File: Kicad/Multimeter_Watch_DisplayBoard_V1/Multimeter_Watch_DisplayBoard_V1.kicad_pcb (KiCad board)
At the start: 2 copper layers, 55 x 46 mm, 21 parts, among them J1 Conn_01x03_Male, J2 Conn_01x03_Male, J3 Conn_01x03_Male, J4 Conn_01x03_Male, Q1 A03400A N-MOS, SW1 SW_Push, SW2 SW_Push, SW3 SW_Push, SW4 SW_Push, SW5 SW_Push, SW6 SW_Push

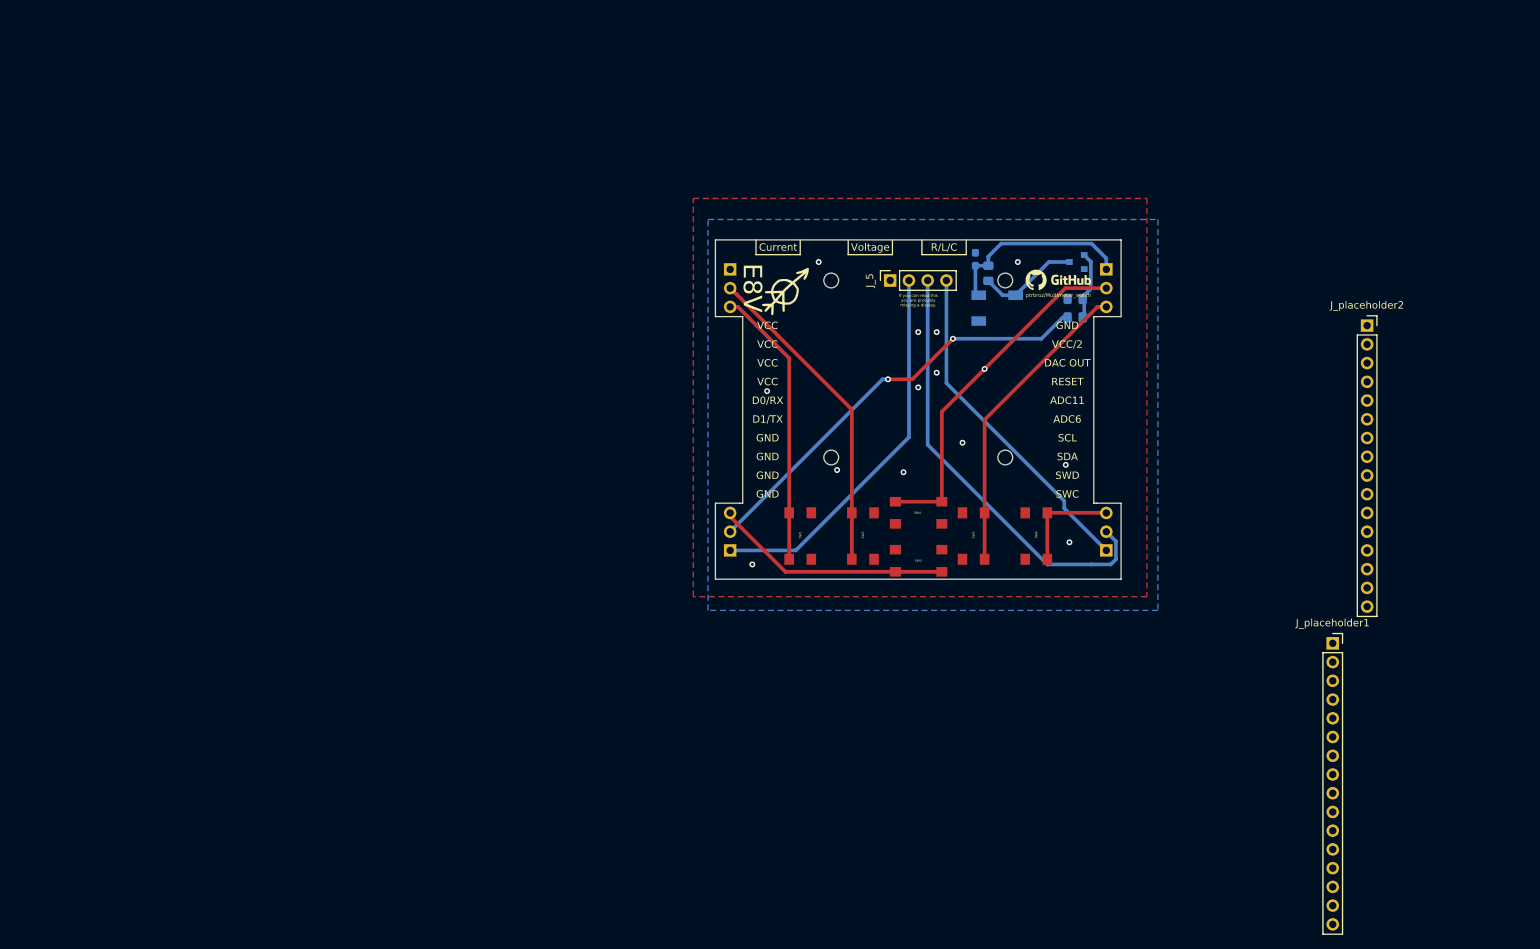
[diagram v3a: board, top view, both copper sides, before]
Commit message: Add pads on bottom of displayboard
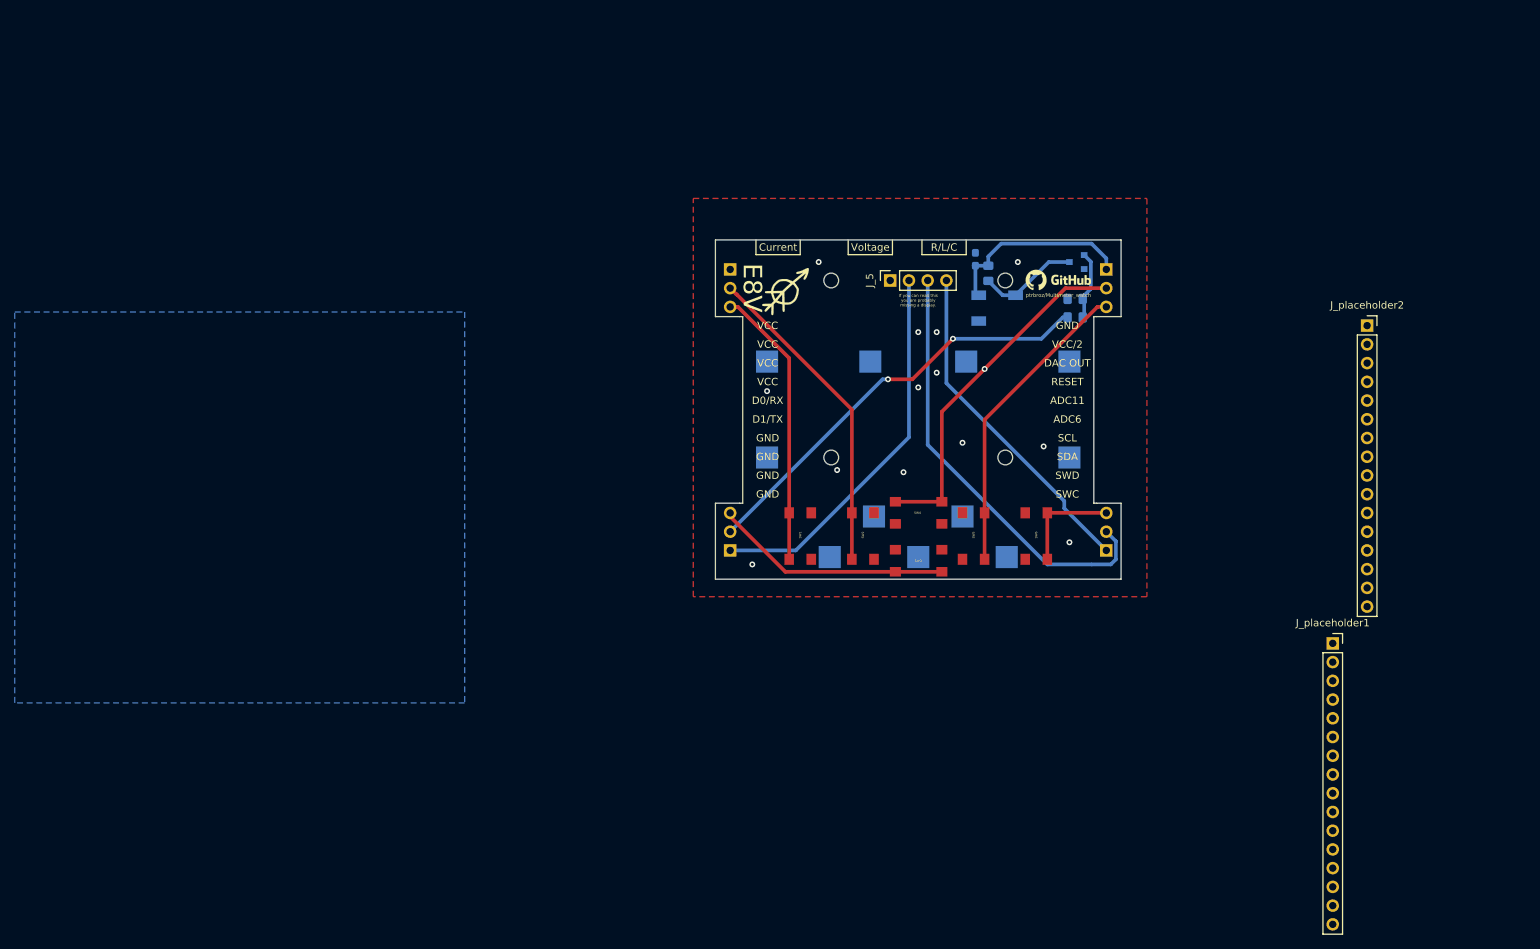
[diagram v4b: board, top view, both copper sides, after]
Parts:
- added REF**: StructPad, Multimeter_Watch_custom_footprints:StructPad, B.Cu at (137.5, 92.5)
- added REF**: StructPad, Multimeter_Watch_custom_footprints:StructPad, B.Cu at (111.0, 71.5)
- added REF**: StructPad, Multimeter_Watch_custom_footprints:StructPad, B.Cu at (152.0, 71.5)
- added REF**: StructPad, Multimeter_Watch_custom_footprints:StructPad, B.Cu at (125.5, 92.5)
- added REF**: StructPad, Multimeter_Watch_custom_footprints:StructPad, B.Cu at (125.0, 71.5)
- added REF**: StructPad, Multimeter_Watch_custom_footprints:StructPad, B.Cu at (138.0, 71.5)
- added REF**: StructPad, Multimeter_Watch_custom_footprints:StructPad, B.Cu at (131.5, 98.0)
- added REF**: StructPad, Multimeter_Watch_custom_footprints:StructPad, B.Cu at (119.5, 98.0)
- added REF**: StructPad, Multimeter_Watch_custom_footprints:StructPad, B.Cu at (143.5, 98.0)
- added REF**: StructPad, Multimeter_Watch_custom_footprints:StructPad, B.Cu at (152.0, 84.5)
- added REF**: StructPad, Multimeter_Watch_custom_footprints:StructPad, B.Cu at (111.0, 84.5)
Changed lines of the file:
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@@
   (general
     (thickness 1.6)
-    (drawings 105)
+    (drawings 106)
     (tracks 80)
     (zones 0)
-    (modules 21)
+    (modules 32)
     (nets 47)
   )
   (page A4)
   (layers
-    (0 F.Cu signal)
-    (31 B.Cu signal hide)
+    (0 F.Cu signal hide)
+    (31 B.Cu signal)
     (32 B.Adhes user hide)
     (33 F.Adhes user hide)
@@
     (38 B.Mask user hide)
     (39 F.Mask user hide)
-    (40 Dwgs.User user hide)
+    (40 Dwgs.User user)
     (41 Cmts.User user hide)
     (42 Eco1.User user)
@@
     (add_net "Net-(J_placeholder2-Pad9)")
     (add_net "Net-(Q1-Pad1)")
+  )
+  (module Multimeter_Watch_custom_footprints:StructPad (layer B.Cu)
+    (at 137.5 92.5)
+    (fp_text reference REF** (at 0 -0.5) (layer B.SilkS)
+      (effects (font (size 1 1) (thickness 0.15)) (justify mirror))
+    )
+    (fp_text value StructPad (at 0 0.5) (layer B.Fab)
+      (effects (font (size 1 1) (thickness 0.15)) (justify mirror))
+    )
+    (pad "" smd rect (at 0 0) (size 3 3) (layers B.Cu B.Paste B.Mask))
+  )
+  (module Multimeter_Watch_custom_footprints:StructPad (layer B.Cu)
+    (at 125.5 92.5)
+    (fp_text reference REF** (at 0 -0.5) (layer B.SilkS)
+      (effects (font (size 1 1) (thickness 0.15)) (justify mirror))
+    )
+    (fp_text value StructPad (at 0 0.5) (layer B.Fab)
+      (effects (font (size 1 1) (thickness 0.15)) (justify mirror))
+    )
+    (pad "" smd rect (at 0 0) (size 3 3) (layers B.Cu B.Paste B.Mask))
+  )
+  (module Multimeter_Watch_custom_footprints:StructPad (layer B.Cu)
+    (at 125 71.5)
+    (fp_text reference REF** (at 0 -0.5) (layer B.SilkS)
+      (effects (font (size 1 1) (thickness 0.15)) (justify mirror))
+    )
+    (fp_text value StructPad (at 0 0.5) (layer B.Fab)
+      (effects (font (size 1 1) (thickness 0.15)) (justify mirror))
+    )
+    (pad "" smd rect (at 0 0) (size 3 3) (layers B.Cu B.Paste B.Mask))
+  )
+  (module Multimeter_Watch_custom_footprints:StructPad (layer B.Cu)
+    (at 138 71.5)
+    (fp_text reference REF** (at 0 -0.5) (layer B.SilkS)
+      (effects (font (size 1 1) (thickness 0.15)) (justify mirror))
+    )
+    (fp_text value StructPad (at 0 0.5) (layer B.Fab)
+      (effects (font (size 1 1) (thickness 0.15)) (justify mirror))
+    )
+    (pad "" smd rect (at 0 0) (size 3 3) (layers B.Cu B.Paste B.Mask))
+  )
+  (module Multimeter_Watch_custom_footprints:StructPad (layer B.Cu)
+    (at 131.5 98)
+    (fp_text reference REF** (at 0 -0.5) (layer B.SilkS)
+      (effects (font (size 1 1) (thickness 0.15)) (justify mirror))
+    )
+    (fp_text value StructPad (at 0 0.5) (layer B.Fab)
+      (effects (font (size 1 1) (thickness 0.15)) (justify mirror))
+    )
+    (pad "" smd rect (at 0 0) (size 3 3) (layers B.Cu B.Paste B.Mask))
+  )
+  (module Multimeter_Watch_custom_footprints:StructPad (layer B.Cu)
+    (at 119.5 98)
+    (fp_text reference REF** (at 0 -0.5) (layer B.SilkS)
+      (effects (font (size 1 1) (thickness 0.15)) (justify mirror))
+    )
+    (fp_text value StructPad (at 0 0.5) (layer B.Fab)
+      (effects (font (size 1 1) (thickness 0.15)) (justify mirror))
+    )
+    (pad "" smd rect (at 0 0) (size 3 3) (layers B.Cu B.Paste B.Mask))
+  )
+  (module Multimeter_Watch_custom_footprints:StructPad (layer B.Cu)
+    (at 143.5 98)
+    (fp_text reference REF** (at 0 -0.5) (layer B.SilkS)
+      (effects (font (size 1 1) (thickness 0.15)) (justify mirror))
+    )
+    (fp_text value StructPad (at 0 0.5) (layer B.Fab)
+      (effects (font (size 1 1) (thickness 0.15)) (justify mirror))
+    )
+    (pad "" smd rect (at 0 0) (size 3 3) (layers B.Cu B.Paste B.Mask))
+  )
+  (module Multimeter_Watch_custom_footprints:StructPad (layer B.Cu)
+    (at 152 84.5)
+    (fp_text reference REF** (at 0 -0.5) (layer B.SilkS)
+      (effects (font (size 1 1) (thickness 0.15)) (justify mirror))
+    )
+    (fp_text value StructPad (at 0 0.5) (layer B.Fab)
+      (effects (font (size 1 1) (thickness 0.15)) (justify mirror))
+    )
+    (pad "" smd rect (at 0 0) (size 3 3) (layers B.Cu B.Paste B.Mask))
+  )
+  (module Multimeter_Watch_custom_footprints:StructPad (layer B.Cu)
+    (at 111 84.5)
+    (fp_text reference REF** (at 0 -0.5) (layer B.SilkS)
+      (effects (font (size 1 1) (thickness 0.15)) (justify mirror))
+    )
+    (fp_text value StructPad (at 0 0.5) (layer B.Fab)
+      (effects (font (size 1 1) (thickness 0.15)) (justify mirror))
+    )
+    (pad "" smd rect (at 0 0) (size 3 3) (layers B.Cu B.Paste B.Mask))
+  )
+  (module Multimeter_Watch_custom_footprints:StructPad (layer B.Cu)
+    (at 111 71.5)
+    (fp_text reference REF** (at 0 -0.5) (layer B.SilkS)
+      (effects (font (size 1 1) (thickness 0.15)) (justify mirror))
+    )
+    (fp_text value StructPad (at 0 0.5) (layer B.Fab)
+      (effects (font (size 1 1) (thickness 0.15)) (justify mirror))
+    )
+    (pad "" smd rect (at 0 0) (size 3 3) (layers B.Cu B.Paste B.Mask))
+  )
+  (module Multimeter_Watch_custom_footprints:StructPad (layer B.Cu)
+    (at 152 71.5)
+    (fp_text reference REF** (at 0 -0.5) (layer B.SilkS)
+      (effects (font (size 1 1) (thickness 0.15)) (justify mirror))
+    )
+    (fp_text value StructPad (at 0 0.5) (layer B.Fab)
+      (effects (font (size 1 1) (thickness 0.15)) (justify mirror))
+    )
+    (pad "" smd rect (at 0 0) (size 3 3) (layers B.Cu B.Paste B.Mask))
   )
   (module Multimeter_Watch_custom_footprints:nouth_signature (layer F.Cu)
@@
     )
   )
+  (dimension 34.5 (width 0.15) (layer Dwgs.User)
+    (gr_text "34.500 mm" (at 80.2 83.75 270) (layer Dwgs.User)
+      (effects (font (size 1 1) (thickness 0.15)))
+    )
+    (feature1 (pts (xy 141.5 101) (xy 80.913579 101)))
+    (feature2 (pts (xy 141.5 66.5) (xy 80.913579 66.5)))
+    (crossbar (pts (xy 81.5 66.5) (xy 81.5 101)))
+    (arrow1a (pts (xy 81.5 101) (xy 80.913579 99.873496)))
+    (arrow1b (pts (xy 81.5 101) (xy 82.086421 99.873496)))
+    (arrow2a (pts (xy 81.5 66.5) (xy 80.913579 67.626504)))
+    (arrow2b (pts (xy 81.5 66.5) (xy 82.086421 67.626504)))
+  )
   (gr_line (start 138 57) (end 138 55) (layer F.SilkS) (width 0.12))
   (gr_line (start 132 57) (end 138 57) (layer F.SilkS) (width 0.12))
@@
   (segment (start 141 60.549999) (end 142.950001 62.5) (width 0.5) (layer B.Cu) (net 1))
   (via (at 140.5 72.5) (size 0.8) (drill 0.4) (layers F.Cu B.Cu) (net 43))
-  (via (at 151.5 85.5) (size 0.8) (drill 0.4) (layers F.Cu B.Cu) (net 2))
+  (via (at 148.5 83) (size 0.8) (drill 0.4) (layers F.Cu B.Cu) (net 2))
   (via (at 111 75.5) (size 0.8) (drill 0.4) (layers F.Cu B.Cu) (net 2))
   (via (at 145 58) (size 0.8) (drill 0.4) (layers F.Cu B.Cu) (net 2))
@@
     (polygon
       (pts
-        (xy 164 105.230776) (xy 103 105.230776) (xy 103 52.230776) (xy 164 52.230776)
+        (xy 70 117.771835) (xy 9 117.771835) (xy 9 64.771835) (xy 70 64.771835)
       )
     )

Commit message: rename pads
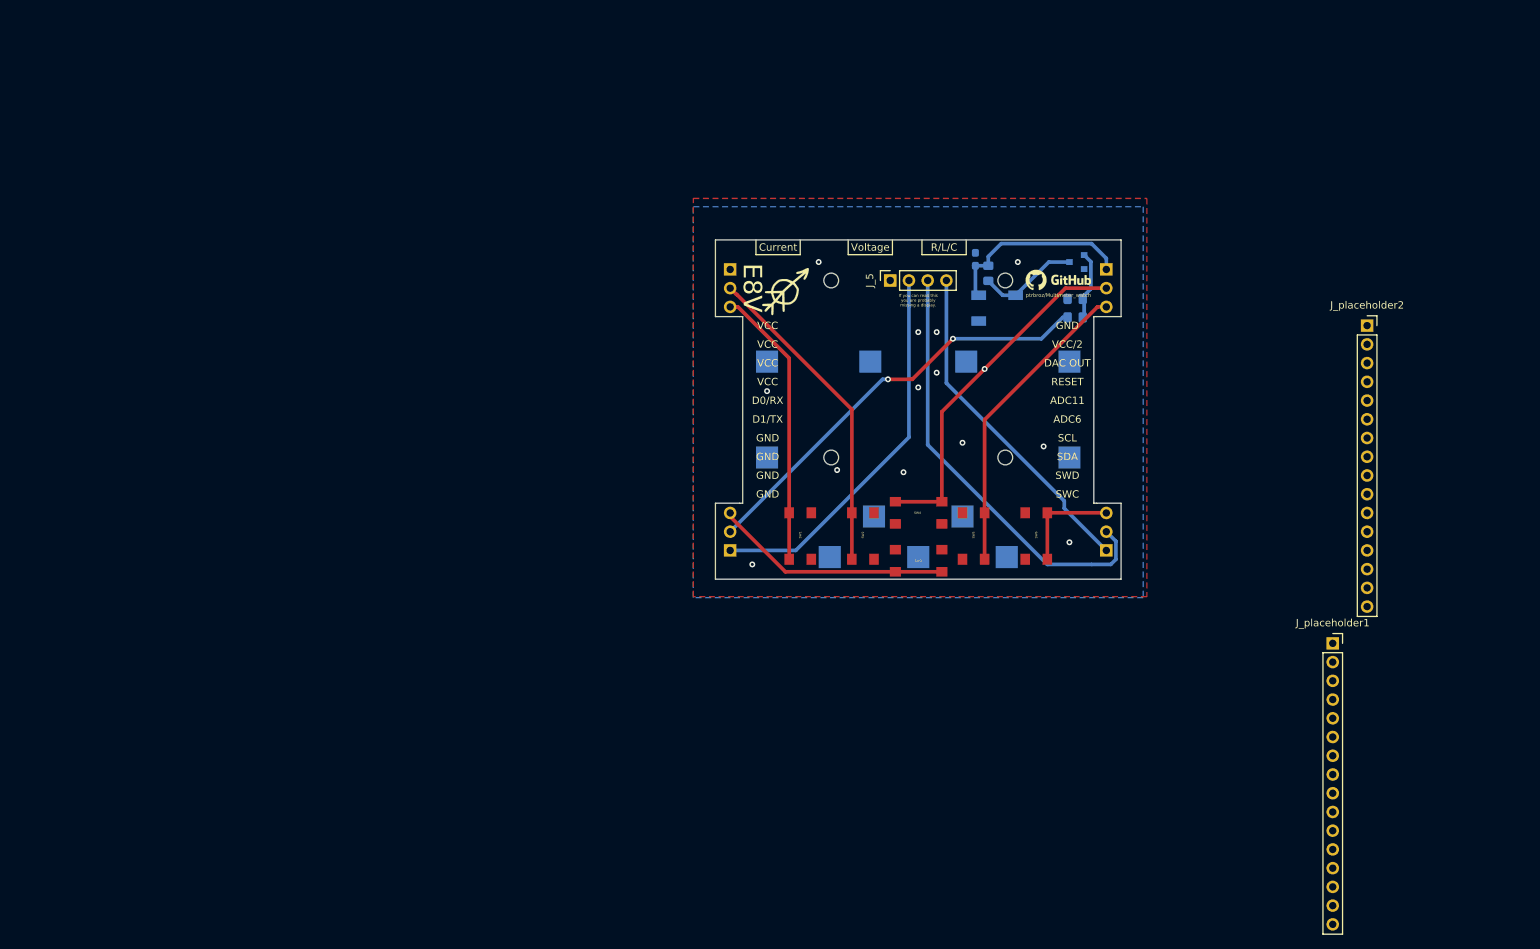
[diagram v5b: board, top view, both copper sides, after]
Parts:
- renumbered REF** to Struct1, REF** to Struct10, REF** to Struct11, REF** to Struct2, REF** to Struct3, REF** to Struct4, REF** to Struct5, REF** to Struct6, REF** to Struct7, REF** to Struct8, REF** to Struct9
